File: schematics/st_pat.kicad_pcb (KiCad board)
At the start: 2 copper layers, 121.9 x 87 mm, 19 parts, among them J4 BATTERY, SW1 SW_PWR, SW2 BTN_RST, SW3 BTN, SW4 BTN, SW5 BTN, U1 GPS_Breakout_746, U2 FEATHER_M0_BASIC_PROTO, U3 LIS2MDL_ADAFRUIT, U4 Sharp_Display_4694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

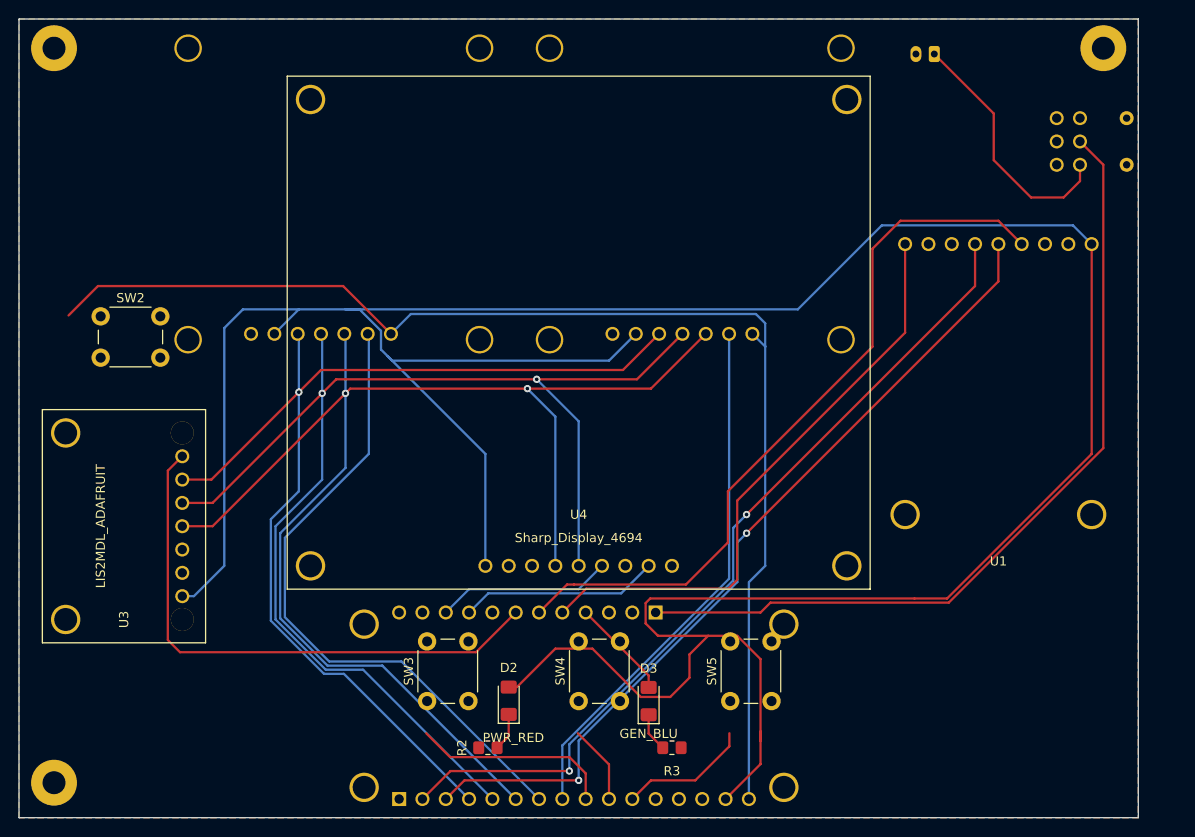
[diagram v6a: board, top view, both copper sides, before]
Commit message: update buttons layout and redo traces; add 3d model for adafruit feather
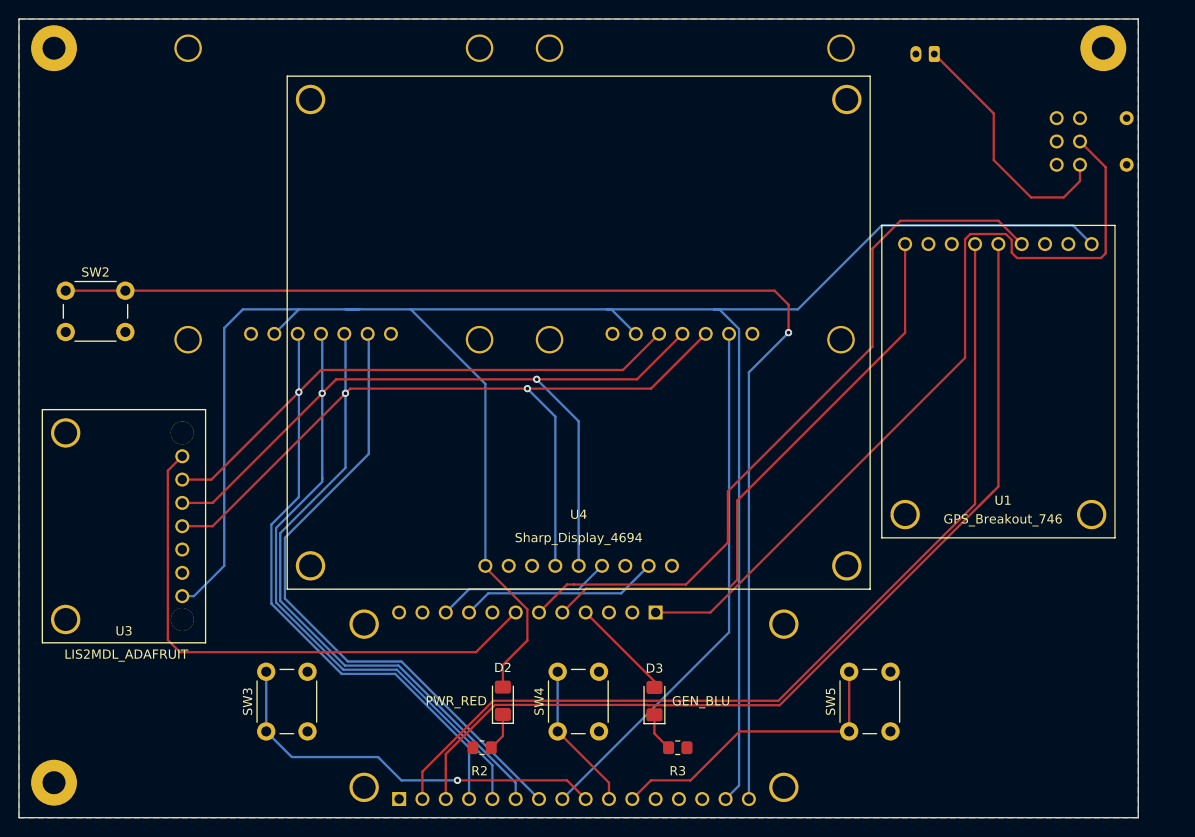
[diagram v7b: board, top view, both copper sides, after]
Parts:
- moved SW3 17.8 mm to (105.7, 115.1)
- moved SW5 13.4 mm to (169.2, 115.1)
- moved SW2 4.72 mm to (83.8, 67.1)
- moved SW4 4.02 mm to (137.4, 115.1)
- moved D2 0.64 mm to (131.4, 111.7)
- moved D3 0.64 mm to (148.0, 111.8)
- moved R2 0.63 mm to (129.2, 116.8)
- moved R3 0.63 mm to (150.5, 116.8)
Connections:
- U5 pad 1: /RST -> (no net)
- U6 pad 1: /RST -> (no net)
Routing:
- net +3V3: track 341.4 -> 244.3 mm
- net /BTN_A3: track 22.0 -> 44.6 mm, vias 0 -> 1
- net /BTN_A1: track 14.4 -> 33.2 mm
- net /GPS_TX: track 92.7 -> 105.8 mm, vias 2 -> 0
- net /GPS_RX: track 93.0 -> 103.6 mm, vias 2 -> 0
- net /BTN_A2: track 8.58 -> 16.2 mm
- net /MISO: track 120.9 -> 123.0 mm
- net +BATT: track 90.6 -> 89.1 mm
- net /MOSI: track 149.5 -> 150.7 mm
- net /SRAD_RECV_CS_A5: track 70.6 -> 69.4 mm
- net /RST: track 135.4 -> 135.5 mm, vias 0 -> 1
